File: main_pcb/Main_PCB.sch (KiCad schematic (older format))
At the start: 59 parts

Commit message: First "finieshed" version of the main pcb schematic
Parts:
- removed J? (x3): US, Connector_PinHeader_2.54mm:PinHeader_2x03_P2.54mm_Horizontal, symbol Connector_Generic:Conn_02x03_Odd_Even
- removed J? (x2): DS, Connector_PinSocket_2.54mm:PinSocket_2x03_P2.54mm_Horizontal, symbol Connector_Generic:Conn_02x03_Odd_Even
- removed J?: ISP, Connector_PinHeader_2.54mm:PinHeader_2x03_P2.54mm_Vertical, symbol Connector_Generic:Conn_02x03_Odd_Even
- removed R?: 33, Resistor_SMD:R_0603_1608Metric, symbol Device:R
- removed R? (x4): ?, Resistor_SMD:R_0603_1608Metric, symbol Device:R
- removed R? (x2): 220, Resistor_SMD:R_0603_1608Metric, symbol Device:R
- removed SW? (x5): SW_Push, symbol Switch:SW_Push
- added C3, C4: 27p, Capacitor_SMD:C_0603_1608Metric, symbol Device:C
- added C7, C8: 100n, Capacitor_SMD:C_0603_1608Metric, symbol Device:C
- added H4: MountingHole_Pad, MountingHole:MountingHole_3.2mm_M3_Pad, symbol Mechanical:MountingHole_Pad
- added J1: DBG, Connector_PinHeader_2.54mm:PinHeader_1x12_P2.54mm_Vertical, symbol Connector_Generic:Conn_01x12
- added J2, J3, J5, J6: UI, Connector_PinHeader_2.54mm:PinHeader_2x02_P2.54mm_Vertical, symbol Connector_Generic:Conn_02x02_Odd_Even
- added J7: UPDN, Connector_PinSocket_2.54mm:PinSocket_2x04_P2.54mm_Vertical, symbol Connector_Generic:Conn_02x04_Odd_Even
- added R13, R2: 1k, Resistor_SMD:R_0603_1608Metric, symbol Device:R
- added R7, R8: 330, Resistor_SMD:R_0603_1608Metric, symbol Device:R
- added SW1: SW_SPST, Button_Switch_THT:SW_PUSH_6mm_H8mm, symbol Switch:SW_SPST
- added Y1: 16 MHz, Crystal:Crystal_SMD_HC49-SD, symbol Device:Crystal
- C2: renamed from C?; value 10n -> 100n; footprint Capacitor_SMD:C_01005_0402Metric -> Capacitor_SMD:C_0603_1608Metric; MPN CC0402KRX7R7BB103 -> CC0603KRX7R0BB104
- J4: renamed from J?; footprint (none) -> Connector_PinSocket_2.54mm:PinSocket_2x20_P2.54mm_Vertical; MPN (none) -> C50982; Manufacturer (none) -> BOOMELE
- Q2: renamed from HSS2307; value Q_PMOS_SGD -> HSS2307; footprint (none) -> Package_TO_SOT_SMD:SOT-23W; MPN (none) -> HSS2307; Manufacturer (none) -> Huashuo
- gave numbers to parts that had none: 38
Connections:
- net labels added: BR+, BR-, DN_RETO, DN_TX, PD2, PI_LED, PI_SHTDN, SP+, SP-, SS, STAT, TRIG, UC_LED, UC_RX, UC_TX, UP_RETO, UP_TX
- net labels removed: DLED, LED, RETI, RETO, RX, RXA, RXB, RXuC, TP1, TRIGI, TRIGO, TX, TXA, TXB, uC_schaltet_den_PI, ~CS, ~HOLD, ~RET_EN, ~WP
- wire segments 118 -> 144
- no-connect marks 5 -> 23
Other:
- note added: "Battery-Management"
- note added: "TODO:\n- Interrupt of UART externer required?"
- note added: "User-Interface"
- note removed: "1 RETO -> RX Master\n2 TRIGI\n3 RX -> TX Master\n4 /\n5 MASTER_ON\n6 GND"
- note removed: "16 MHz Quarz nehmen\nHC49"
- note removed: "2s auf low für ein\n"
- note removed: "Batterie-Überwachung"
- note removed: "Flash - nötig?"
- note removed: "LED sind auf der Vorderseite der Tochter-platinen"
- note removed: "LOW for SPI"
- note removed: "PI SPI\nSPI Header Pin Pin Name Pin Function\n\nMOSI 19 GPIO10 SPI0_MOSI\nMISO 21 GPIO09 SPI0_MISO\nSCLK 23 GPIO11 SPI0_SCLK\nCE0 24 GPIO08 SPI0_CE0_N\nCE1 26 GPIO07 SPI0_CE1_N"
- note removed: "Stecker zu Board auf 8 Pin ändern\n\nFemale-Header"
- note removed: "UART PI-Intern"
- note removed: "passt der Dropout von leerer Batt auf 5V?"
- moved on the sheet: C14, C15, C2, C5, D1, H1, H2, H3, J8, R1, R12, R14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

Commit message: Initial placement of components, replaced Step-Down with LDO due to lack of supplies
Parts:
- removed C10, C11, C5: 22u, Capacitor_SMD:C_0603_1608Metric, symbol Device:C
- removed C9: 100n, Capacitor_SMD:C_0603_1608Metric, symbol Device:C
- removed L1: 4.7u, Inductor_SMD:L_Abracon_ASPI-0630LR, symbol Device:L
- removed R16: 54.9k, Resistor_SMD:R_0603_1608Metric, symbol Device:R
- removed R17: 10k, Resistor_SMD:R_0603_1608Metric, symbol Device:R
- removed U2: TPS563200, Package_TO_SOT_SMD:SOT-23-6, symbol Regulator_Switching:TPS563200
- C14: value 22u -> 10u; footprint Capacitor_SMD:C_0603_1608Metric -> Capacitor_SMD:C_1206_3216Metric; MPN CC0603MRX5R5BB226 -> CC1206KKX5R8BB106
- C15: footprint Capacitor_SMD:C_0603_1608Metric -> Capacitor_SMD:C_1206_3216Metric; MPN CC0603MRX5R5BB226 -> CC1206KKX5R8BB226
- J4: footprint Connector_PinSocket_2.54mm:PinSocket_2x20_P2.54mm_Vertical -> main_pcb:RPiZero
- J8: footprint Connector_PinHeader_2.54mm:PinHeader_2x03_P2.54mm_Vertical -> Connector_IDC:IDC-Header_2x03_P2.54mm_Vertical; MPN 210-72-03GB01 -> C9135; Manufacturer PINREX -> BOOMELE
- U4: value AP1117-33 -> AZ1117-50; symbol Regulator_Linear:AP1117-33 -> Regulator_Linear:AZ1117-5.0; MPN AP1117E33G-13 -> AZ1117CH-5.0TRG1
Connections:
- net +3V3: no longer C15.1, U4.2 (VO)
- net +5V: now also C15.1, U4.2 (VO)
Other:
- note removed: "Spannungsregler 3,3 V Festspannung"
- note removed: "wenn Strom aus dem Pi ausreicht, dann weg lassen"
- moved on the sheet: C14, C15, H1, H2, H3, H4, U4

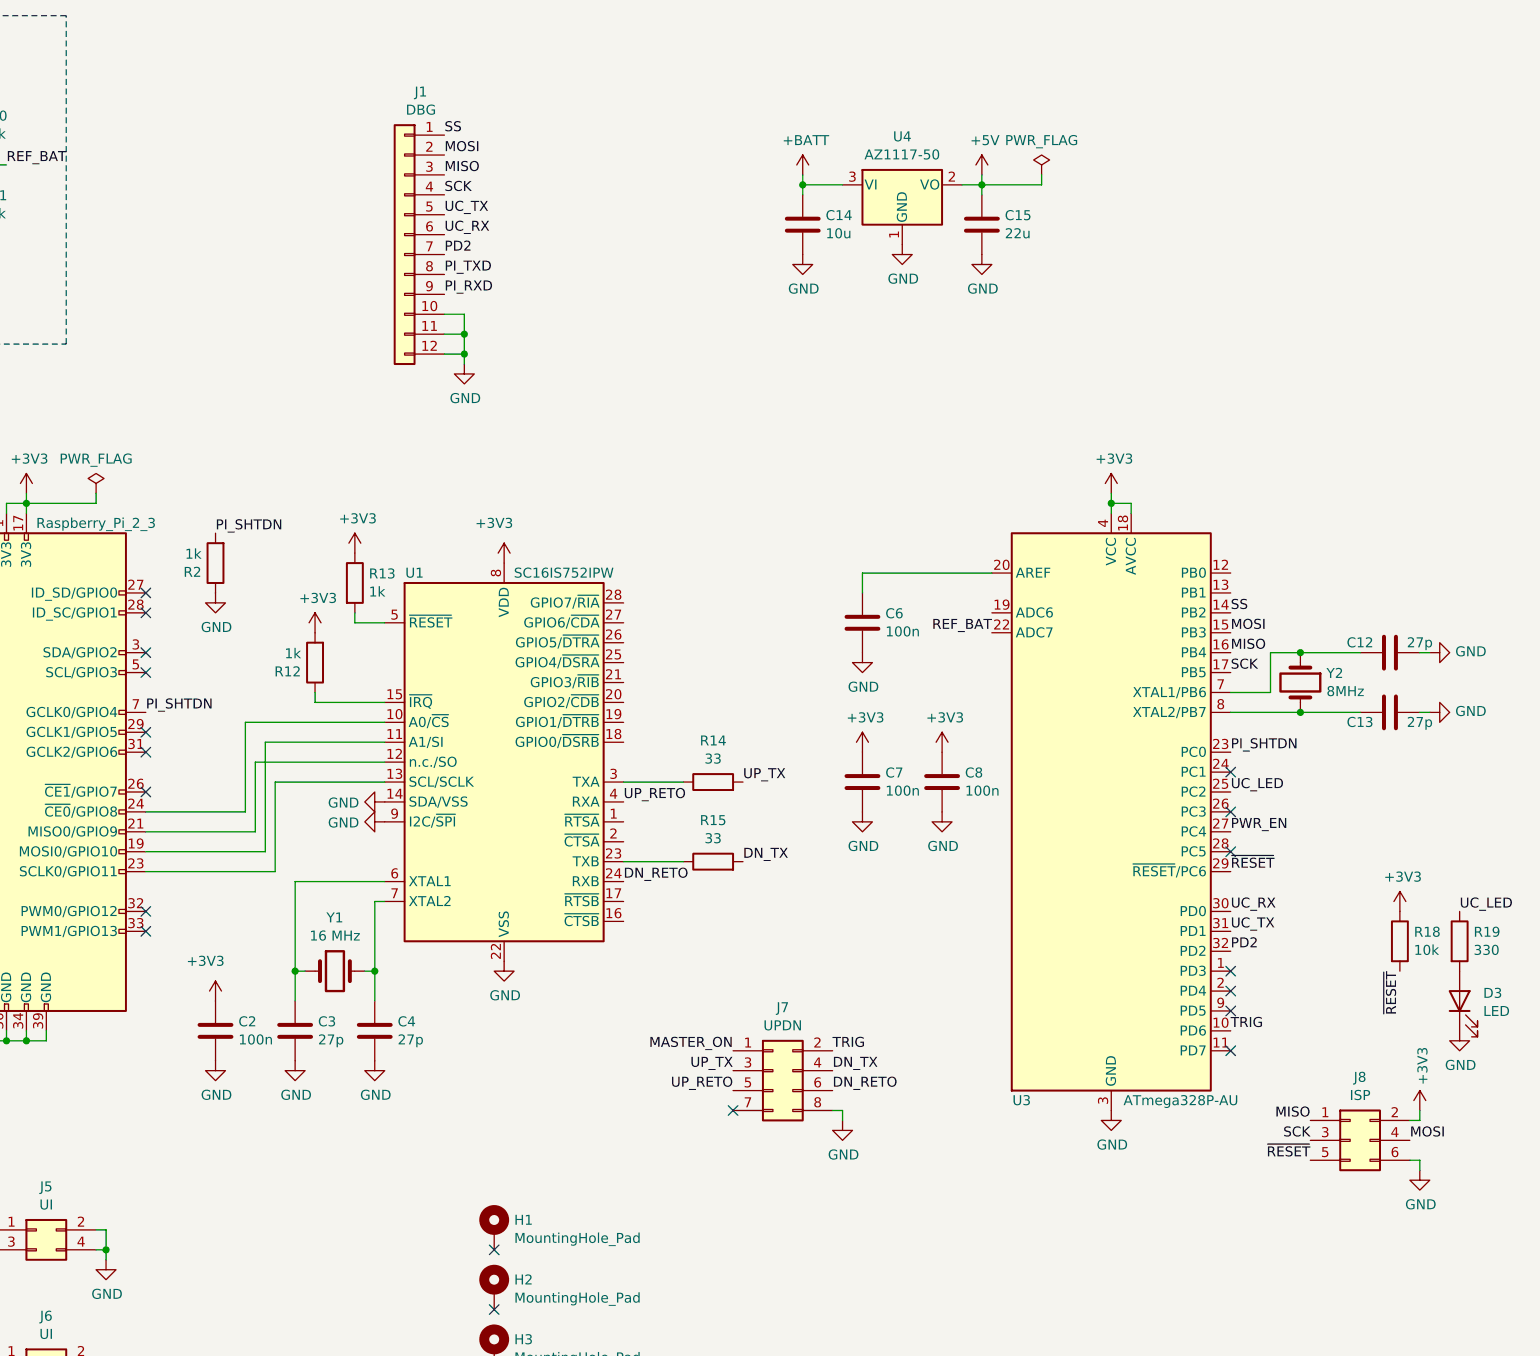
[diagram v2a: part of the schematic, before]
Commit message: Added I2C connection between pi and avr, just in case
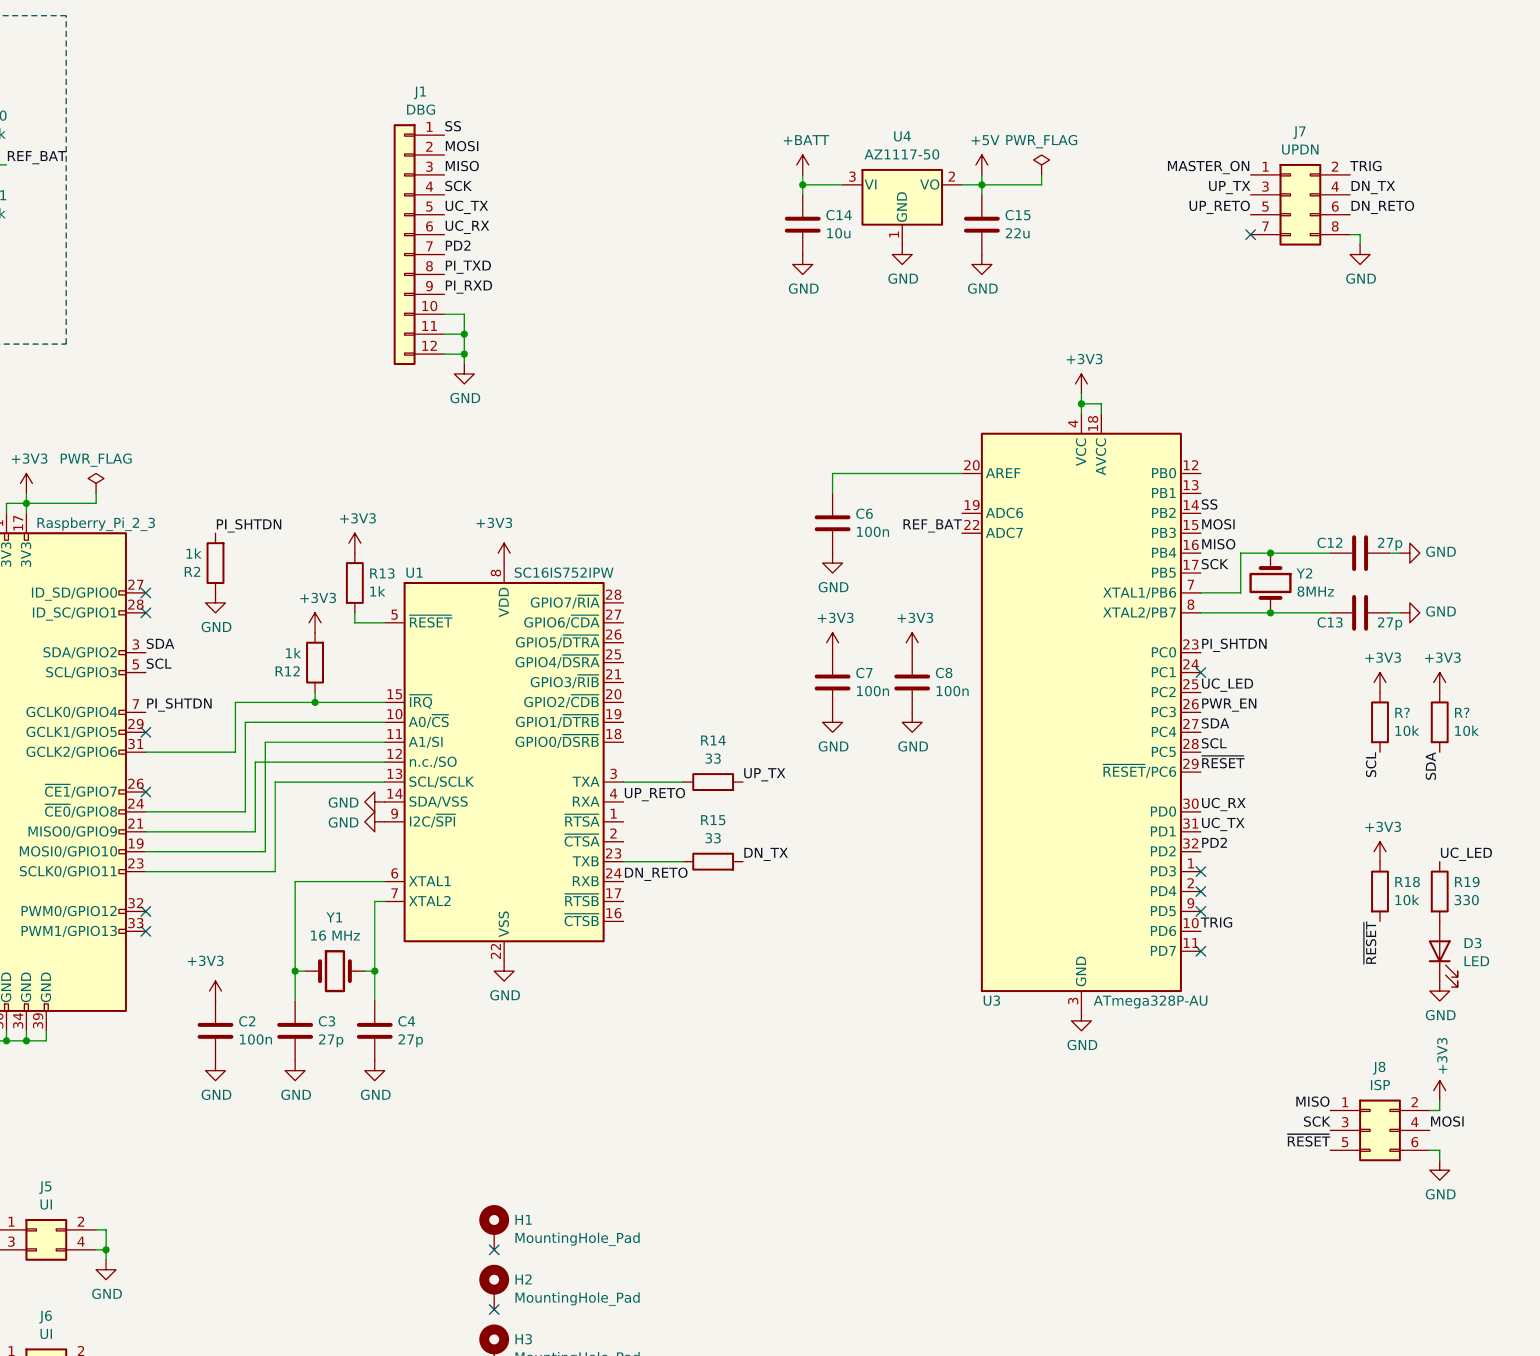
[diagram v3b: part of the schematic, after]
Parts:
- added R? (x2): 10k, Resistor_SMD:R_0603_1608Metric, symbol Device:R
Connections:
- net +3V3: now also R?.1, R?.1
- net PWR_EN: now also U3.26 (PC3); no longer U3.27 (PC4)
- net at R12.1, U1.15 (~IRQ): now also J4.31 (GCLK2/GPIO6)
- net SDA: now reaches J4.3 (SDA/GPIO2)
- net SDA: now also U3.27 (PC4), R?.2
- net SCL: now reaches J4.5 (SCL/GPIO3)
- net SCL: now also U3.28 (PC5), R?.2
- no-connect marks 23 -> 18
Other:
- moved on the sheet: C12, C13, C6, C7, C8, D3, J7, J8, R18, R19, U3, Y2

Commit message: Intial routing of main pcb
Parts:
- J4: value Raspberry_Pi_2_3 -> Raspberry_Pi_Zero_WH
- gave numbers to parts that had none: 2
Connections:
- net BR-: now also J4.32 (PWM0/GPIO12); no longer J4.37 (GPIO26)
- net STAT: now also J4.33 (PWM1/GPIO13); no longer J4.18 (GPIO24)
- net TRIG: no longer J3.4 (Pin_4)
- net ~SC_IRQ: now reaches R12.1, U1.15 (~IRQ)
- net ~SC_IRQ: now also J4.18 (GPIO24); no longer J4.31 (GCLK2/GPIO6)
- net BTN_TRIG: now reaches J4.27 (ID_SD/GPIO0)
- net BTN_TRIG: now also J3.4 (Pin_4)
- no-connect marks 18 -> 17
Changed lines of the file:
@@
 P 3550 4300
 F 0 "J4" H 2900 5550 50  0000 C CNN
-F 1 "Raspberry_Pi_2_3" H 4100 5550 50  0000 C CNN
+F 1 "Raspberry_Pi_Zero_WH" H 4200 5550 50  0000 C CNN
 F 2 "main_pcb:RPiZero" H 3550 4300 50  0001 C CNN
 F 3 "https://www.raspberrypi.org/documentation/hardware/raspberrypi/schematics/rpi_SCH_3bplus_1p0_reduced.pdf" H 3550 4300 50  0001 C CNN
@@
 Wire Wire Line
 	3350 5650 3450 5650
-NoConn ~ 4350 3400
 NoConn ~ 4350 3500
 NoConn ~ 4350 4100
@@
 Connection ~ 2550 7350
 Text Label 3100 7350 0    50   ~ 0
-TRIG
+BTN_TRIG
 Text Label 3100 6600 0    50   ~ 0
 SP+
@@
 Text Label 2750 4800 2    50   ~ 0
 BR+
-Text Label 2750 4700 2    50   ~ 0
+Text Label 4350 5100 0    50   ~ 0
 STAT
-Text Label 2750 4900 2    50   ~ 0
+Text Label 4350 5000 0    50   ~ 0
 BR-
 $Comp
@@
 Text Notes 800  2550 0    50   ~ 0
 TODO:\n- Interrupt of UART externer required?
-NoConn ~ 4350 5000
-NoConn ~ 4350 5100
 NoConn ~ 9650 3800
 NoConn ~ 9650 4800
@@
 Wire Wire Line
 	5200 3950 4800 3950
-Wire Wire Line
-	4800 3950 4800 4200
-Wire Wire Line
-	4800 4200 4350 4200
 Connection ~ 5200 3950
 NoConn ~ 9650 5000
@@
 SCL
 $Comp
-L power:+3V3 #PWR?
+L power:+3V3 #PWR03
 U 1 1 617EB094
 P 10850 3900
-F 0 "#PWR?" H 10850 3750 50  0001 C CNN
+F 0 "#PWR03" H 10850 3750 50  0001 C CNN
 F 1 "+3V3" H 10865 4073 50  0000 C CNN
 F 2 "" H 10850 3900 50  0001 C CNN
@@
 $EndComp
 $Comp
-L Device:R R?
+L Device:R R4
 U 1 1 617EB09C
 P 10850 4050
-F 0 "R?" H 10920 4096 50  0000 L CNN
+F 0 "R4" H 10920 4096 50  0000 L CNN
 F 1 "10k" H 10920 4005 50  0000 L CNN
 F 2 "Resistor_SMD:R_0603_1608Metric" V 10780 4050 50  0001 C CNN
@@
 $EndComp
 $Comp
-L power:+3V3 #PWR?
+L power:+3V3 #PWR02
 U 1 1 61814088
 P 10550 3900
-F 0 "#PWR?" H 10550 3750 50  0001 C CNN
+F 0 "#PWR02" H 10550 3750 50  0001 C CNN
 F 1 "+3V3" H 10565 4073 50  0000 C CNN
 F 2 "" H 10550 3900 50  0001 C CNN
@@
 $EndComp
 $Comp
-L Device:R R?
+L Device:R R3
 U 1 1 61814090
 P 10550 4050
-F 0 "R?" H 10620 4096 50  0000 L CNN
+F 0 "R3" H 10620 4096 50  0000 L CNN
 F 1 "10k" H 10620 4005 50  0000 L CNN
 F 2 "Resistor_SMD:R_0603_1608Metric" V 10480 4050 50  0001 C CNN
@@
 Text Label 10550 4200 3    50   ~ 0
 SCL
+Text Label 4800 3950 0    50   ~ 0
+~SC_IRQ
+Text Label 2750 4700 2    50   ~ 0
+~SC_IRQ
+Text Label 4350 3400 0    50   ~ 0
+BTN_TRIG
+NoConn ~ 4350 4200
+NoConn ~ 2750 4900
 $EndSCHEMATC
